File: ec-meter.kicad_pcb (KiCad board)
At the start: 2 copper layers, 50.8 x 76.2 mm, 35 parts, among them P1 Probe, P2 V+, P3 OUT, P4 V-, U1 LM324, U2 LM324

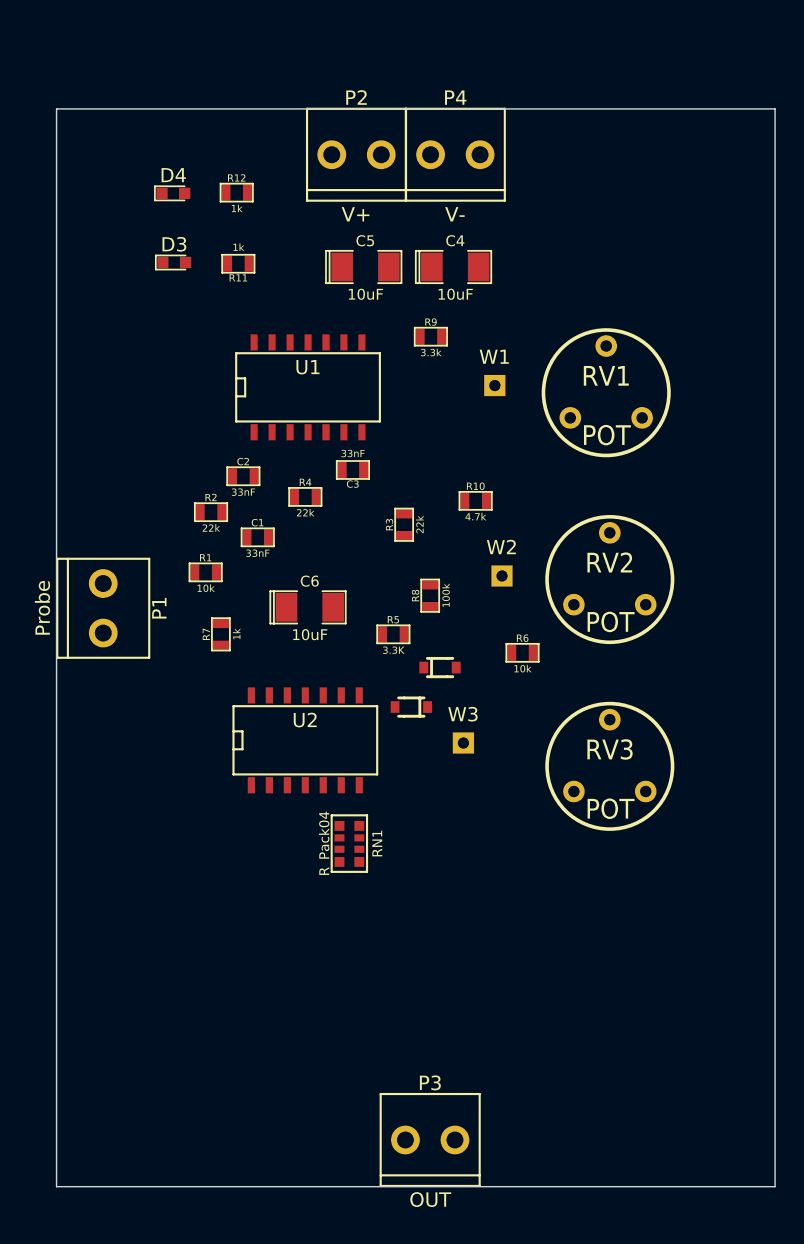
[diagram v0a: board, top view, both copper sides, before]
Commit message: Moved parts, rearranged opamps
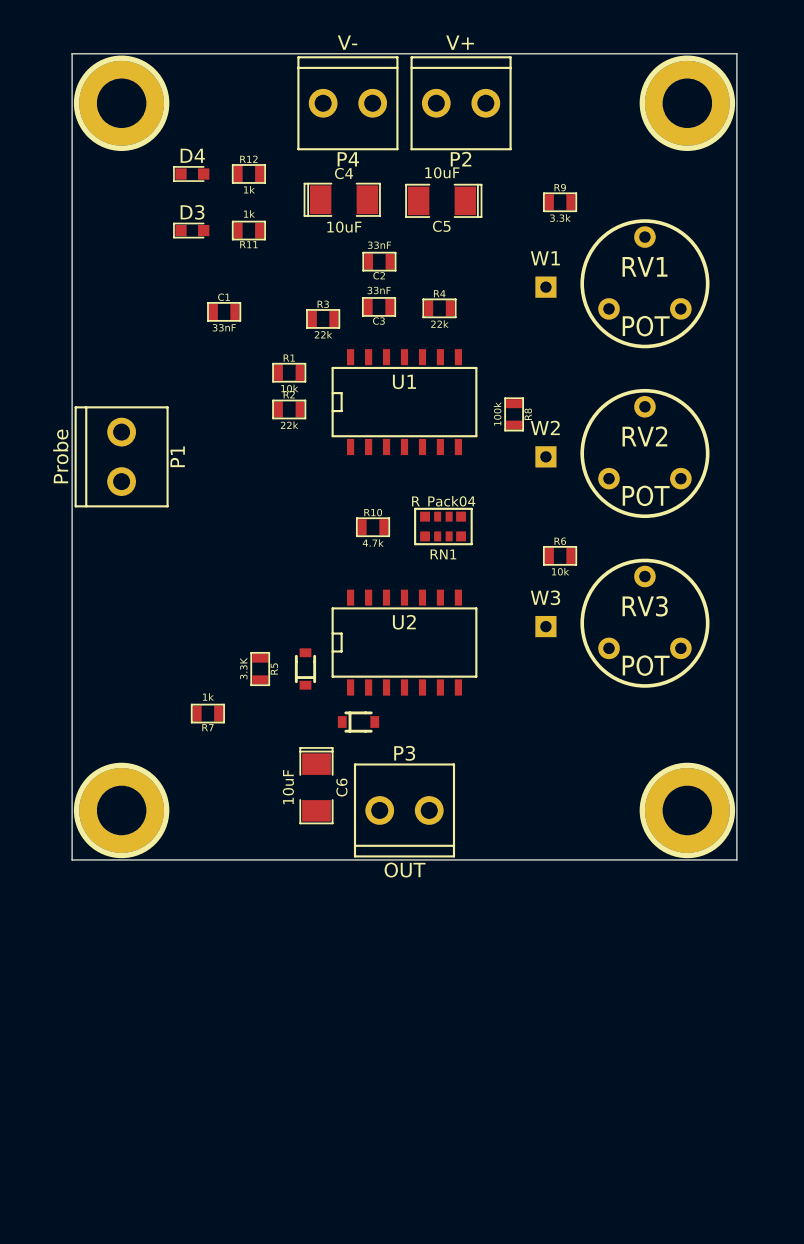
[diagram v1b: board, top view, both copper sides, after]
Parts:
- added h?: pin, visgence_parts:1pin_C, F.Cu at (30.0, 25.0)
- added h?: pin, visgence_parts:1pin_C, F.Cu at (70.0, 25.0)
- added h?: pin, visgence_parts:1pin_C, F.Cu at (30.0, 75.0)
- added h?: pin, visgence_parts:1pin_C, F.Cu at (70.0, 75.0)
- moved RN1 23.4 mm to (52.8, 54.9), turned to 0 degrees
- moved P3 23.4 mm to (50.0, 75.0)
- moved C2 18.0 mm to (48.2, 36.2), turned to 180 degrees
- moved R4 16.4 mm to (52.5, 39.5)
- moved C1 16.1 mm to (37.2, 39.8)
- moved R3 15.6 mm to (44.2, 40.2), turned to 0 degrees
- moved R1 15.3 mm to (41.9, 44.0)
- moved R8 14.1 mm to (57.8, 47.0), turned to 270 degrees
- moved R9 13.2 mm to (61.0, 32.0)
- moved C6 12.7 mm to (43.8, 73.4), turned to 270 degrees
- moved C3 11.7 mm to (48.2, 39.4)
- moved P1 10.8 mm to (30.0, 50.0)
- moved RV3 10.4 mm to (67.0, 61.0)
- moved W3 10.1 mm to (60.0, 62.0)
- moved U2 9.85 mm to (50.0, 63.0)
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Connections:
- RV1 pad 1: (no net) -> Net-(RV1-Pad1)
- RV2 pad 3: (no net) -> Net-(RV2-Pad3)
- RV3 pad 3: (no net) -> Net-(RV3-Pad3)
- U1 pad 1: Net-(C2-Pad1) -> SineOut
- U1 pad 10: Net-(R8-Pad2) -> GND
- U1 pad 12: (no net) -> Net-(C1-Pad2)
- U1 pad 13: (no net) -> Net-(C2-Pad2)
- U1 pad 14: (no net) -> Net-(C2-Pad1)
- U1 pad 2: Net-(C2-Pad2) -> SineOut
- U1 pad 3: Net-(C1-Pad2) -> Net-(R8-Pad2)
- U1 pad 5: GND -> (no net)
- U1 pad 6: Net-(C3-Pad2) -> (no net)
- U1 pad 7: Net-(C3-Pad1) -> (no net)
- U1 pad 8: SineOut -> Net-(C3-Pad1)
- U1 pad 9: SineOut -> Net-(C3-Pad2)
- U2 pad 1: Net-(R10-Pad1) -> Net-(D1-Pad2)
- U2 pad 10: Diffout -> Net-(RN1-Pad7)
- U2 pad 12: Net-(C6-Pad1) -> Net-(R8-Pad2)
- U2 pad 13: ECOut -> Probe
- U2 pad 14: ECOut -> Net-(R10-Pad1)
- U2 pad 2: Probe -> Net-(D1-Pad1)
- U2 pad 3: Net-(R8-Pad2) -> Diffout
- U2 pad 5: Net-(RN1-Pad7) -> Net-(C6-Pad1)
- U2 pad 6: Net-(RN1-Pad5) -> ECOut
- U2 pad 7: Diffout -> ECOut
- U2 pad 8: Net-(D1-Pad2) -> Diffout
- U2 pad 9: Net-(D1-Pad1) -> Net-(RN1-Pad5)
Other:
- board size 50.8 x 76.2 mm -> 47 x 57 mm

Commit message: minor layout
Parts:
- moved RN1 0.96 mm to (53.0, 54.0)
- moved R10 0.23 mm to (48.0, 55.0)
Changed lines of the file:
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@@
   )
   (module visgence_parts:RESARRAY-0612 (layer F.Cu)
-    (at 52.75 54.925)
+    (at 53 54)
     (fp_text reference RN1 (at 0 2) (layer F.SilkS)
       (effects (font (size 0.7 0.7) (thickness 0.125)))
@@
   )
   (module visgence_parts:SM0603_VIS (layer F.Cu)
-    (at 47.775 54.975)
+    (at 48 55)
     (attr smd)
     (fp_text reference R10 (at 0 -1.016) (layer F.SilkS)

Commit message: Did routing
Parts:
- C1, C2, C3: footprint visgence_parts:SM0603_VIS -> visgence_parts:SM1206_VIS
- D1, D2: footprint visgence_parts:SOD-323 -> Diodes_SMD:D_SOD-323_HandSoldering
- moved R3 13.2 mm to (57.2, 42.8), turned to 90 degrees
- moved R8 12.5 mm to (58.0, 34.5), turned to 0 degrees
- moved R10 11.3 mm to (59.2, 54.2)
- moved R6 10.6 mm to (59.8, 67.5)
- moved C1 8.61 mm to (41.0, 47.5)
- moved R4 7.05 mm to (46.5, 35.8)
- moved R2 5.96 mm to (41.0, 40.8)
- moved C3 5.05 mm to (53.2, 39.5)
- moved R7 4.84 mm to (40.8, 69.5), turned to 0 degrees
- moved C2 3.72 mm to (46.5, 39.5), turned to 0 degrees
- moved R9 2.55 mm to (61.5, 34.5)
- moved U2 2.00 mm to (50.0, 61.0)
- moved D1 1.90 mm to (46.0, 67.0)
- moved C4 1.08 mm to (46.8, 31.5), turned to 180 degrees
- moved R5 1.04 mm to (39.5, 64.0)
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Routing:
- net GND: track 0.00 -> 236.7 mm, vias 0 -> 2
- net +5V: track 0.00 -> 96.6 mm, vias 0 -> 2
- net -5V: track 0.00 -> 69.4 mm, vias 0 -> 3
- net Probe: track 0.00 -> 48.7 mm
- net Net-(R8-Pad2): track 0.00 -> 40.4 mm
- net SineOut: track 0.00 -> 34.0 mm, vias 0 -> 2
- net Net-(D1-Pad1): track 0.00 -> 32.1 mm
- net Diffout: track 0.00 -> 28.1 mm, vias 0 -> 2
- net AmpOut: track 0.00 -> 25.5 mm, vias 0 -> 1
- net Net-(C1-Pad2): track 0.00 -> 22.1 mm
- net Net-(R10-Pad1): track 0.00 -> 18.2 mm
- net Net-(C3-Pad1): track 0.00 -> 17.9 mm
- net Net-(C6-Pad1): track 0.00 -> 17.1 mm
- net Net-(C3-Pad2): track 0.00 -> 15.3 mm
- net Net-(C2-Pad2): track 0.00 -> 12.8 mm
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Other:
- net class Default: trace_width 0.25 -> 0.635

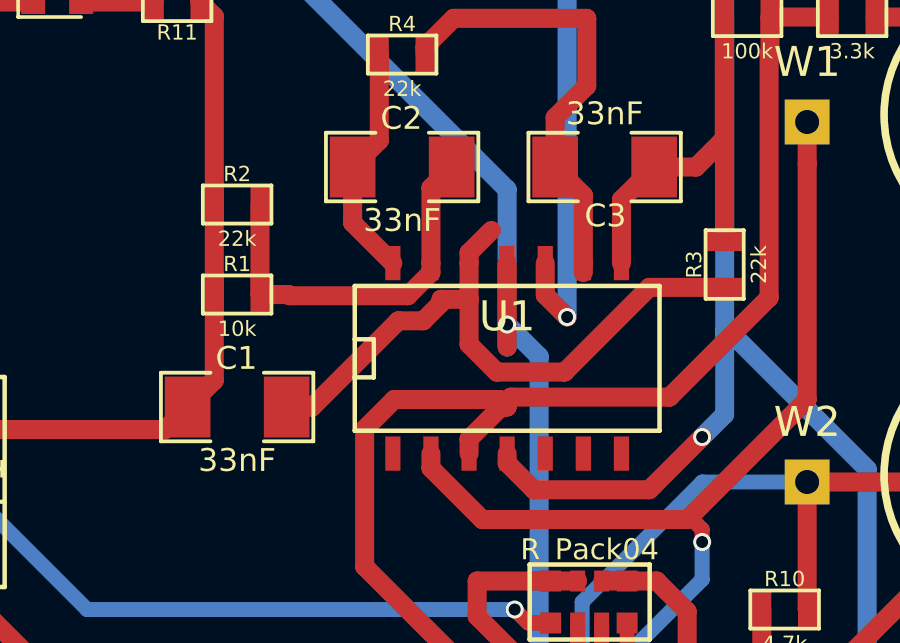
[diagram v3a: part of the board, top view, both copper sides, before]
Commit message: Fixed missing track
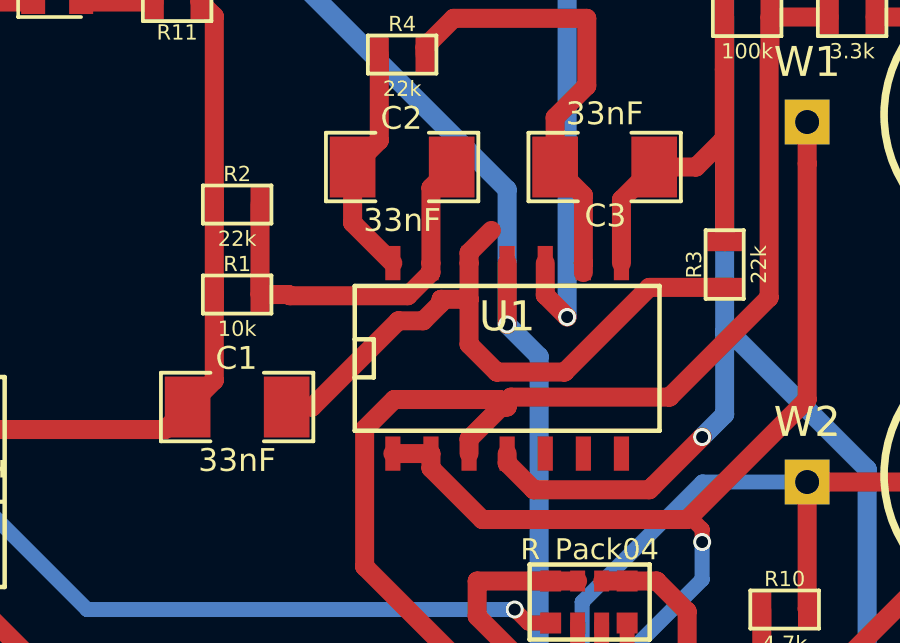
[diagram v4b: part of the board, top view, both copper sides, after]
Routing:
- net -5V: track 69.4 -> 67.9 mm
- net SineOut: track 34.0 -> 35.3 mm
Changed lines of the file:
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@@
   (general
     (links 69)
-    (no_connects 3)
+    (no_connects 0)
     (area 26.449999 21.449999 73.550001 78.550001)
     (thickness 1.6)
     (drawings 7)
-    (tracks 266)
+    (tracks 267)
     (zones 0)
     (modules 39)
@@
   )
   (layers
-    (0 F.Cu signal hide)
-    (31 B.Cu signal hide)
+    (0 F.Cu signal)
+    (31 B.Cu signal)
     (32 B.Adhes user)
     (33 F.Adhes user)
@@
   (segment (start 48.2145 34.5435) (end 52.654002 34.5435) (width 0.635) (layer F.Cu) (net 6))
   (segment (start 52.54 43.0195) (end 52.54 42.702) (width 0.635) (layer F.Cu) (net 6))
+  (segment (start 50 44.75) (end 50 42.702) (width 0.635) (layer F.Cu) (net 7))
+  (segment (start 50 40.25) (end 50 44.75) (width 0.635) (layer B.Cu) (net 7))
   (segment (start 32.75 34) (end 34.2 34) (width 0.635) (layer F.Cu) (net 7))
   (segment (start 44.74994 24.75) (end 42 24.75) (width 0.635) (layer B.Cu) (net 7))
@@
   (segment (start 51.250012 59.075736) (end 51.500012 59.325736) (width 0.635) (layer B.Cu) (net 7))
   (via (at 51.500012 59.75) (size 0.6) (drill 0.4) (layers F.Cu B.Cu) (net 7))
-  (segment (start 50 45.5) (end 50 40.25) (width 0.635) (layer B.Cu) (net 7))
   (segment (start 50 40.25) (end 43 33.25) (width 0.635) (layer B.Cu) (net 7))
   (segment (start 43 33.25) (end 43 26.49994) (width 0.635) (layer B.Cu) (net 7))
   (segment (start 43 26.49994) (end 44.74994 24.75) (width 0.635) (layer B.Cu) (net 7))
-  (segment (start 50 42.702) (end 50 45.5) (width 0.635) (layer F.Cu) (net 7))
   (via (at 50 44.75) (size 0.6) (drill 0.4) (layers F.Cu B.Cu) (net 7))
   (segment (start 44.74994 24.75) (end 44.74994 31.15094) (width 0.635) (layer F.Cu) (net 7))
@@
   (segment (start 60 50) (end 60 54.238) (width 0.635) (layer F.Cu) (net 21))
   (segment (start 60 54.238) (end 60.012 54.25) (width 0.635) (layer F.Cu) (net 21))
+  (segment (start 47.46 49.052) (end 46.19 49.052) (width 0.635) (layer F.Cu) (net 22))
   (segment (start 56.5 52) (end 56.5 51.575736) (width 0.5) (layer F.Cu) (net 22))
   (segment (start 56.5 51.575736) (end 56.174264 51.25) (width 0.5) (layer F.Cu) (net 22))

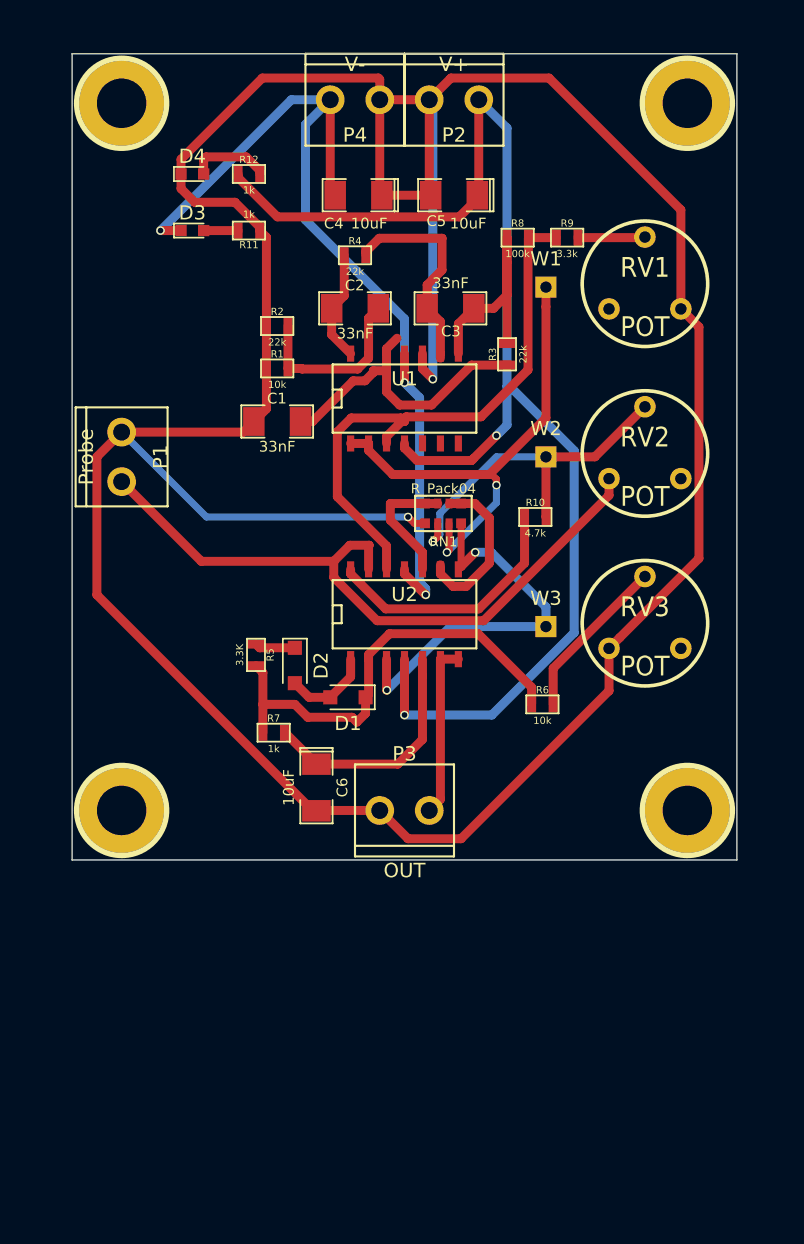
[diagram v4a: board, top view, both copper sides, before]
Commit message: Filled and added some labels
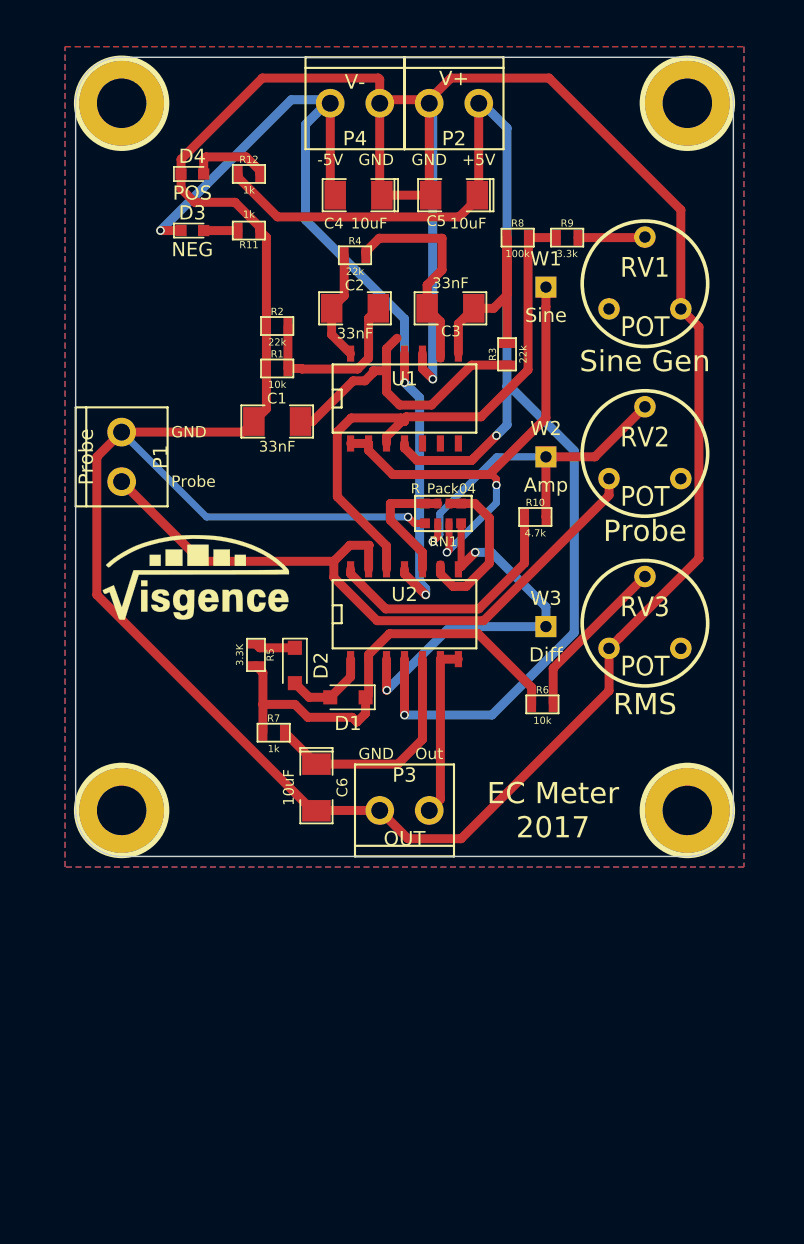
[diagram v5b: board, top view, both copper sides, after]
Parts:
- added G***: LOGO, visgence_parts:LOGO_SMALL, F.Cu at (35.2, 58.5)
- added G***: LOGO, visgence_parts:LOGO_BIG, B.Cu at (50.0, 50.0)
- moved P2 0.25 mm to (53.5, 25.0)
- moved P4 0.25 mm to (46.5, 25.0)
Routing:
- added copper zone on B.Cu, net GND
- added copper zone on F.Cu, net GND
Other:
- board size 47 x 57 mm -> 46.5 x 56.5 mm
- board text added: "+5V"
- board text added: "-5V"
- board text added: "EC Meter 2017"
- board text added: "GND"
- board text added: "Out"
- board text added: "Probe"
- board text added: "RMS"
- board text added: "Sine Gen"

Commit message: final routing
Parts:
- moved D4 0.25 mm to (35.0, 29.8)
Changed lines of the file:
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@@
     (links 69)
     (no_connects 0)
-    (area 26.699999 21.699999 73.300001 78.300001)
+    (area 22.899999 20.899999 74.100001 81.100001)
     (thickness 1.6)
     (drawings 23)
@@
   )
   (module LEDs:LED_0603 (layer F.Cu)
-    (at 35 30)
+    (at 35 29.75)
     (descr "LED 0603 smd package")
     (tags "LED led 0603 SMD smd SMT smt smdled SMDLED smtled SMTLED")
